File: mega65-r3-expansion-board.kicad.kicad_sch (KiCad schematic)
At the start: 0 parts

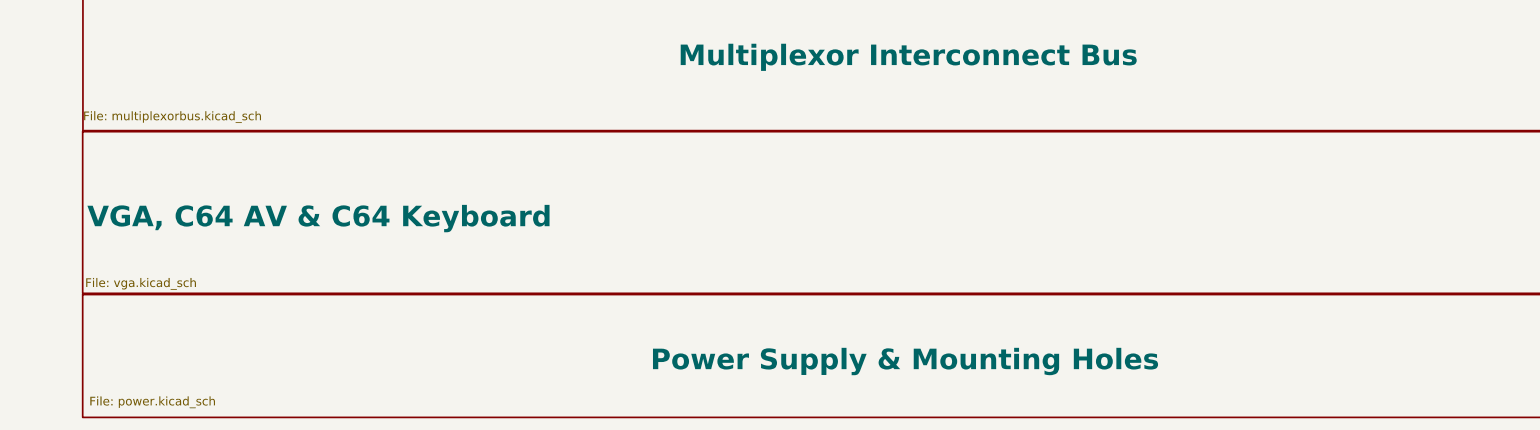
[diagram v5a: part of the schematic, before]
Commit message: fix spi1_o -> sp1_o and route net
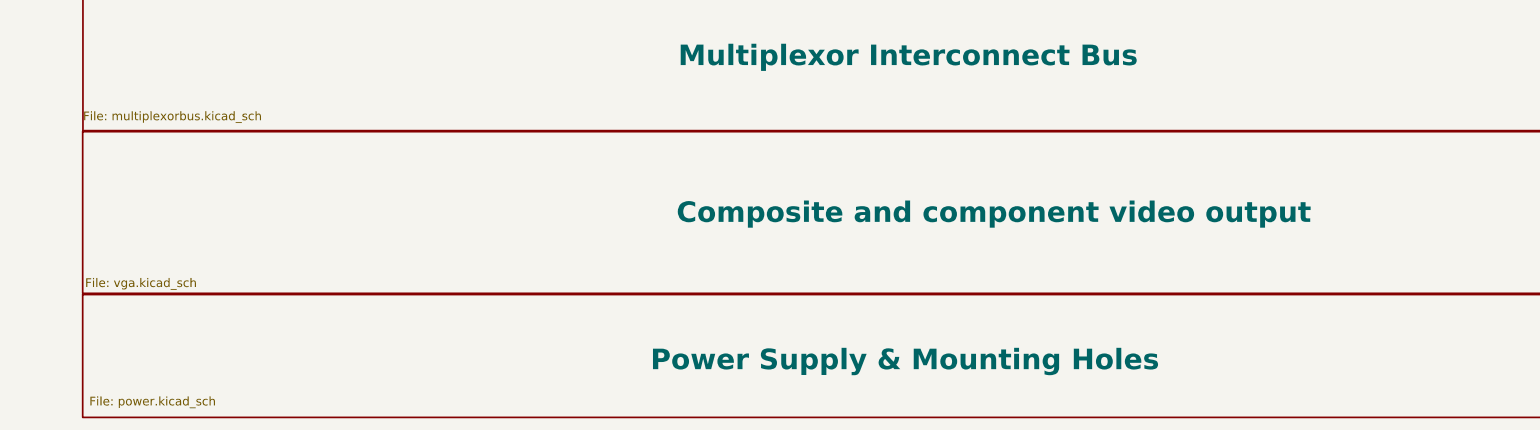
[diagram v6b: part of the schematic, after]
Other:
- sheet VGA, C64 AV & C64 Keyboard renamed Composite and component video output
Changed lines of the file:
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@@
     (stroke (width 0.25) (type solid) (color 0 0 0 0))
     (fill (color 255 208 70 1.0000))
-    (property "Sheet name" "VGA, C64 AV & C64 Keyboard" (id 0) (at 26.67 127.635 0)
+    (property "Sheet name" "Composite and component video output" (id 0) (at 113.03 127 0)
       (effects (font (size 3 3) bold) (justify left bottom))
     )
